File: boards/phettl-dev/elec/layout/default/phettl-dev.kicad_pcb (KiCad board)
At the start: 4 copper layers, 2 parts, among them U1 ?

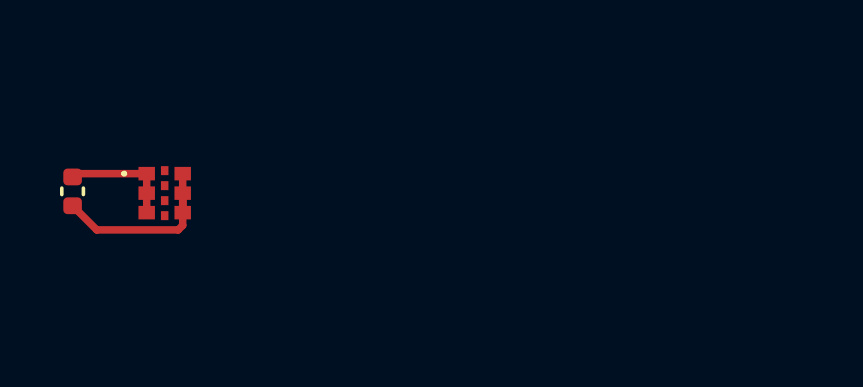
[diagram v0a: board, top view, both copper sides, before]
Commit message: [PART] use better temp sensor
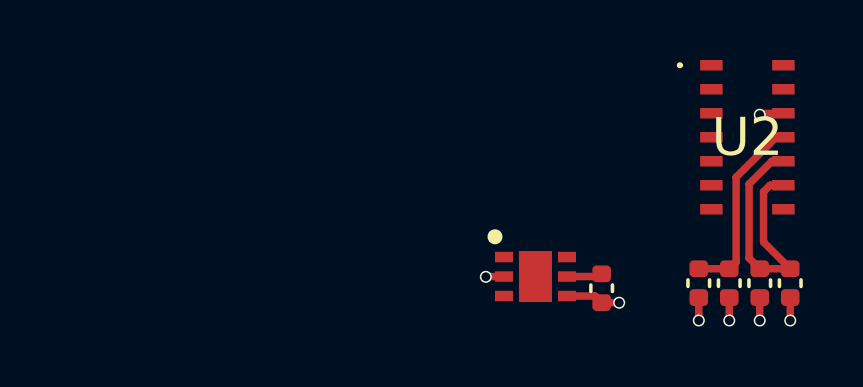
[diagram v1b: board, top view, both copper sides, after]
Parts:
- added C2: 6.3V 10uF X5R ±20% 0402 Multilayer Ceramic Capacitors MLCC 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, lib:C0402, F.Cu at (150.3, 91.9)
- added C3: 16V 100nF X7R ±10% 0402 Multilayer Ceramic Capacitors MLCC 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, lib:C0402, F.Cu at (151.3, 91.9)
- added C4: 10V 4.7uF X5R ±20% 0402 Multilayer Ceramic Capacitors MLCC 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, lib:C0402, F.Cu at (152.4, 91.9)
- added C5: 16V 100nF X7R ±10% 0402 Multilayer Ceramic Capacitors MLCC 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, lib:C0402, F.Cu at (153.4, 91.9)
- added U2: ?, lib:MAX30102EFDT, F.Cu at (151.9, 87.0)
- U1: footprint lib:MAX30208CLBT -> lib:SON65P200X200X80-7N
- moved C1 17.9 mm to (147.1, 92.0)
- moved U1 12.7 mm to (144.9, 91.6)
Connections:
- C1 pad 1: vcc -> temp-vcc
- U1 pad 1: vcc -> temp-scl
- U1 pad 2: vcc -> temp-gnd
- U1 pad 3: vcc -> temp-io
- U1 pad 5: temp-gnd -> temp-vcc
- U1 pad 6: temp-gnd -> temp-sda
- U1 pad 7: temp-io -> ep
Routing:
- net hr-vcc-1: track 0.00 -> 9.13 mm
- net hr-vcc: track 0.00 -> 6.29 mm
- net temp-gnd: track 6.44 -> 2.44 mm, vias 0 -> 2
- net hr-gnd: track 0.00 -> 3.82 mm, vias 0 -> 5
- net vcc: track 3.82 -> 0.00 mm
- net temp-vcc: track 0.00 -> 1.19 mm

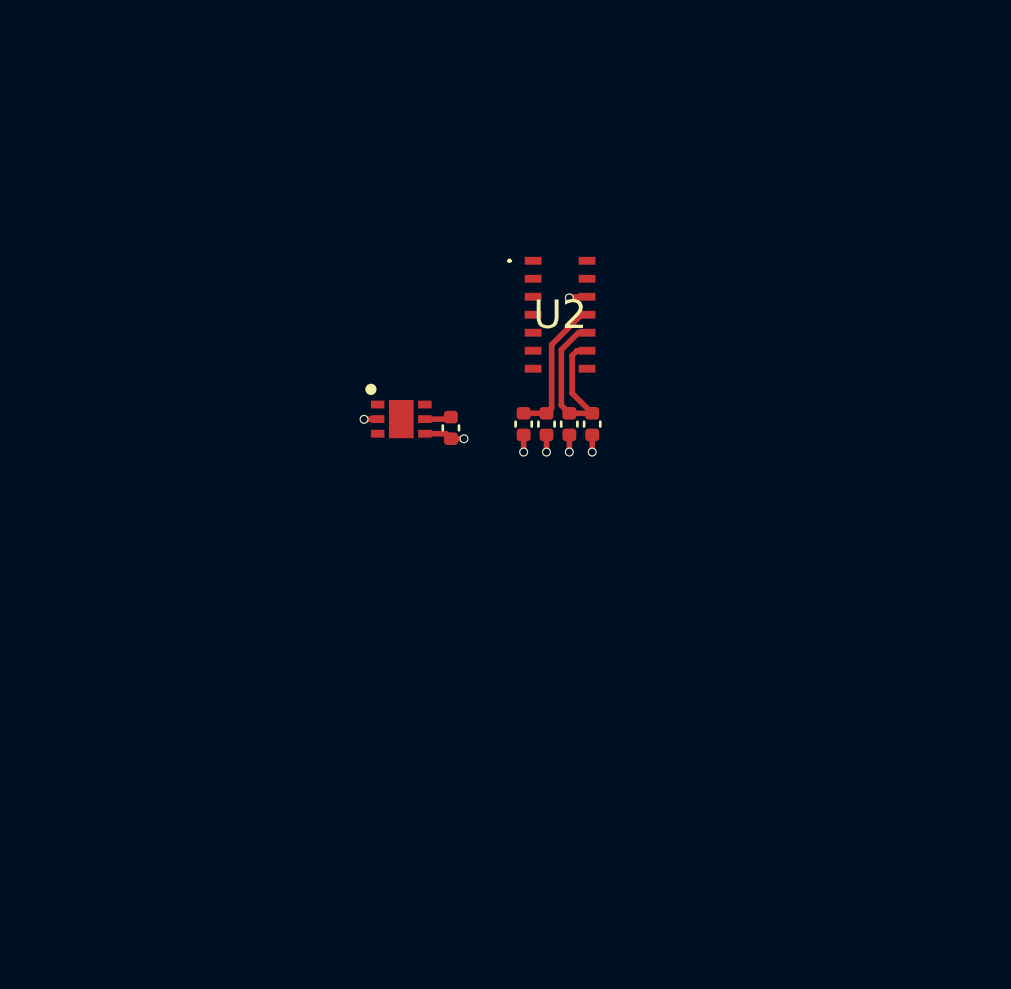
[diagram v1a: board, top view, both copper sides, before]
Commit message: [PART] add xiao
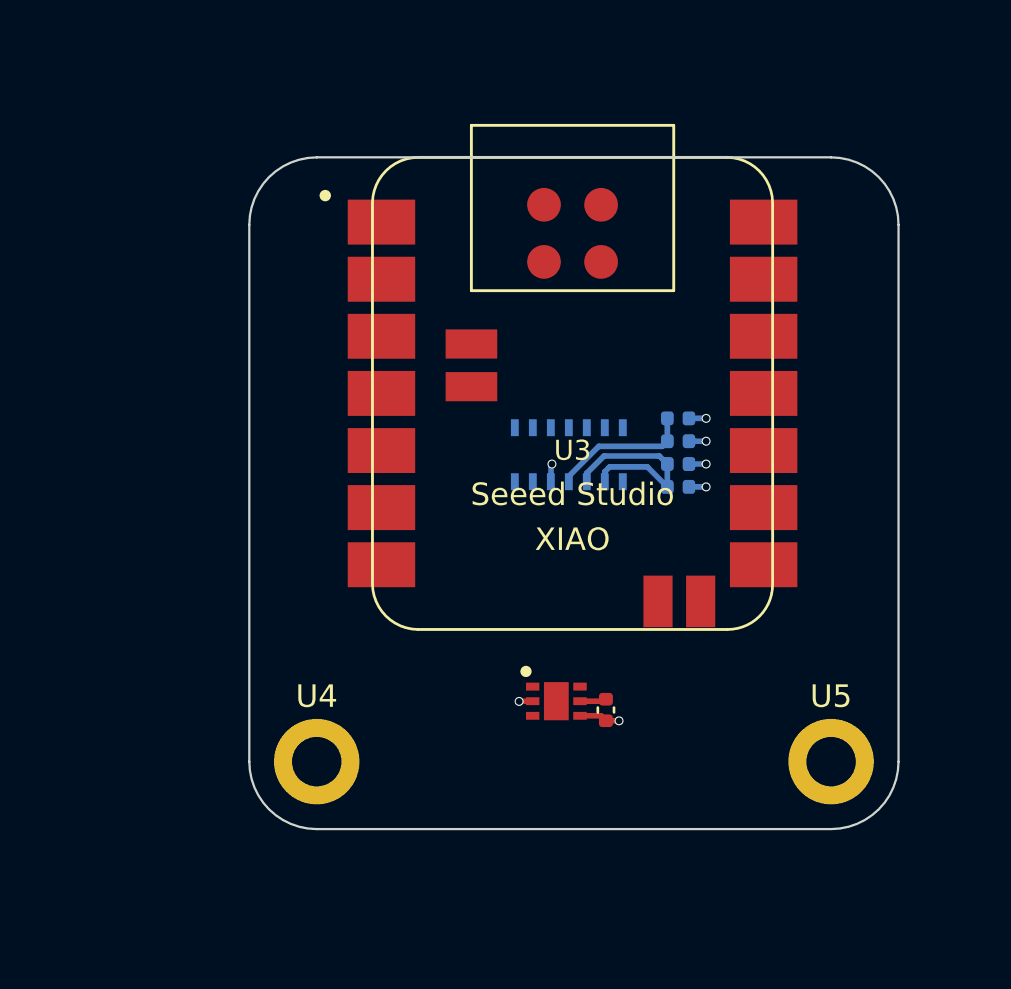
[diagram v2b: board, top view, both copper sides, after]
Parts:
- added U3: ?, lib:XIAO-nRF52840-Sense-14P-2.54-21X17.8MM, F.Cu at (152.5, 90.5)
- added U4: ?, MountingHole:MountingHole_2.2mm_M2_DIN965_Pad, F.Cu at (141.1, 106.9)
- added U5: ?, MountingHole:MountingHole_2.2mm_M2_DIN965_Pad, F.Cu at (164.0, 106.9)
- C2, C3, C4, C5, U2: moved to B.Cu
- moved U1 14.3 mm to (151.8, 104.2)
- moved C1 14.3 mm to (154.0, 104.6)
- moved C2 6.88 mm to (157.2, 91.6), turned to 0 degrees
- moved U2 6.24 mm to (152.3, 93.2), turned to -90 degrees
- moved C3 5.91 mm to (157.2, 92.6), turned to 0 degrees
- moved C4 5.16 mm to (157.2, 93.6), turned to 0 degrees
- moved C5 4.74 mm to (157.2, 94.7), turned to 0 degrees
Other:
- board outline added: 28.9 x 29.9 mm

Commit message: [BOARD] add pullups
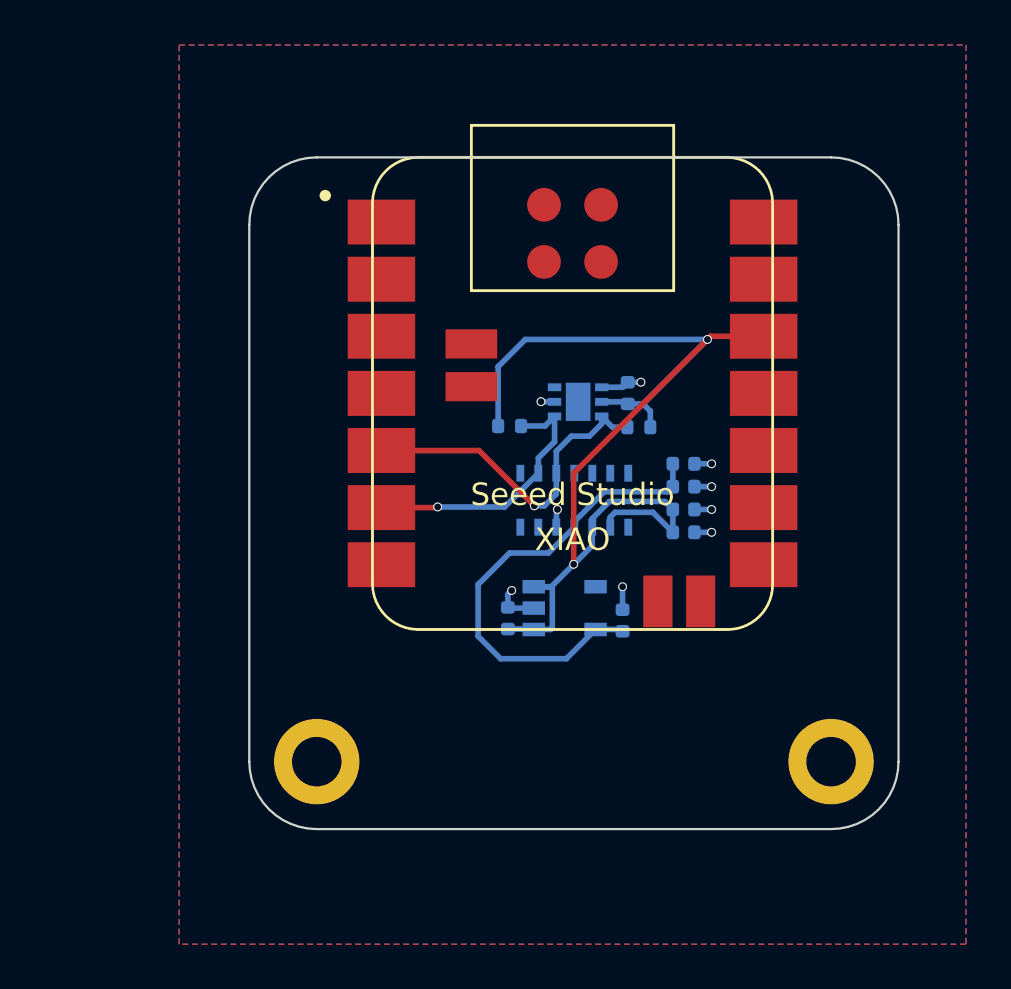
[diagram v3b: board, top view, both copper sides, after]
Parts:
- added C6: 25V 1uF X5R ±10% 0402 Multilayer Ceramic Capacitors MLCC - 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, lib:C0402, B.Cu at (149.6, 100.5)
- added C7: 25V 1uF X5R ±10% 0402 Multilayer Ceramic Capacitors MLCC - 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, lib:C0402, B.Cu at (154.7, 100.6)
- added R1: 62.5mW Thick Film Resistors 50V ±100ppm/℃ ±1% 4.7kΩ 0402 Ch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, lib:R0402, B.Cu at (149.7, 92.0)
- added R2: 62.5mW Thick Film Resistors 50V ±100ppm/℃ ±1% 4.7kΩ 0402 Ch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, lib:R0402, B.Cu at (155.4, 92.0)
- added U6: ?, lib:DBV0005A_N, B.Cu at (152.2, 100.0)
- C1: moved to B.Cu
- U3: renamed from U1; moved to B.Cu
- moved C1 14.1 mm to (155.0, 90.5), turned to 90 degrees
- moved U3 13.4 mm to (152.8, 90.9)
- moved C3 2.04 mm to (157.4, 94.6)
- moved C5 2.04 mm to (157.4, 96.7)
- moved C2 2.04 mm to (157.4, 93.6)
- moved C4 2.04 mm to (157.4, 95.7)
- moved U4 2.04 mm to (152.6, 95.2)
- renumbered U4 to U1, U5 to U2, U2 to U4, U3 to U5
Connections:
- net _5v renamed xiao-vcc
- net batplus renamed vcc
- net hr-vcc renamed vcc-2
- C1 pad 1: temp-vcc -> vcc-1
- C1 pad 2: temp-gnd -> gnd
- C2 pad 2: hr-gnd -> gnd
- C3 pad 2: hr-gnd -> gnd
- C4 pad 1: hr-vcc-1 -> vcc-1
- C4 pad 2: hr-gnd -> gnd
- C5 pad 1: hr-vcc-1 -> vcc-1
- C5 pad 2: hr-gnd -> gnd
- U1 pad 1: m1-gnd -> gnd
- U2 pad 1: m2-gnd -> gnd
- U3 pad 1: temp-scl -> scl
- U3 pad 2: temp-gnd -> gnd
- U3 pad 4: temp-gnd -> gnd
- U3 pad 5: temp-vcc -> vcc-1
- U3 pad 6: temp-sda -> sda
- U4 pad 10: hr-vcc-1 -> vcc-1
- U4 pad 12: hr-gnd -> gnd
- U4 pad 2: hr-scl -> scl
- U4 pad 3: hr-sda -> sda
- U4 pad 9: hr-vcc-1 -> vcc-1
- U5 pad 12: _3v3 -> vcc-1
- U5 pad 13: xiao.ic-gnd -> gnd
- U5 pad 18: xiao.ic-gnd -> gnd
- U5 pad 21: batminus -> gnd
- U5 pad 5: p004_a4_d4_sda -> sda
- U5 pad 6: p005_a5_d5_scl -> scl
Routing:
- net vcc-1: track 0.00 -> 52.5 mm, vias 0 -> 2
- net sda: track 0.00 -> 15.1 mm, vias 0 -> 1
- net vcc-2: track 6.29 -> 21.3 mm
- net scl: track 0.00 -> 12.1 mm, vias 0 -> 1
- net gnd: track 0.00 -> 9.31 mm, vias 0 -> 9
- net hr-vcc-1: track 9.13 -> 0.00 mm
- net hr-gnd: track 3.82 -> 0.00 mm, vias 5 -> 0
- net temp-gnd: track 2.44 -> 0.00 mm, vias 2 -> 0
- net temp-vcc: track 1.19 -> 0.00 mm
- added copper zone on B.Cu, net gnd
- added copper zone on F.Cu, net gnd
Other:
- copper layers 4 -> 2

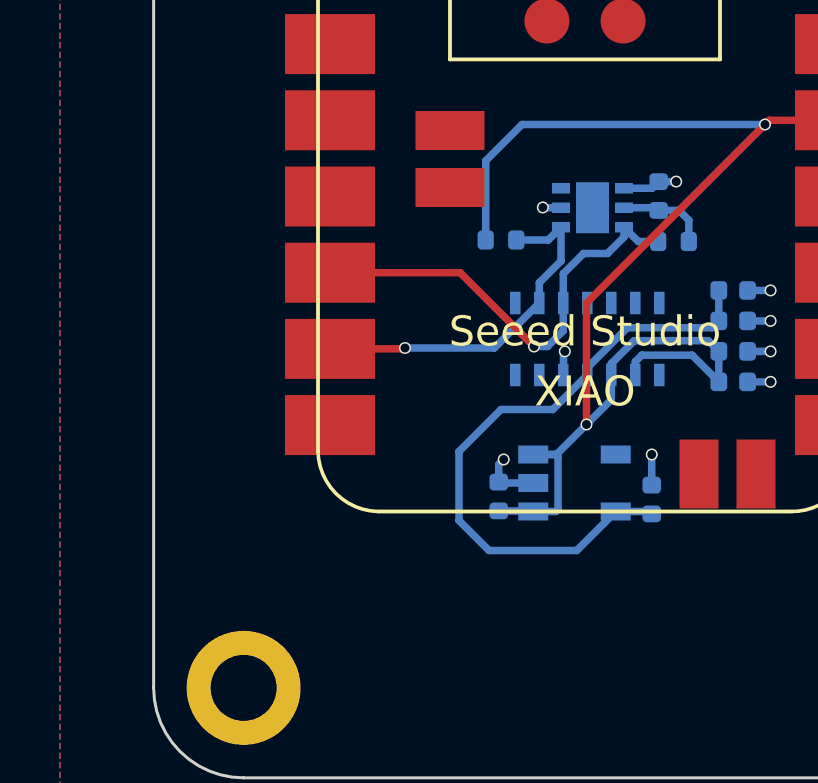
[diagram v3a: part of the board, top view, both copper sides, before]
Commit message: [BAT] add connectors
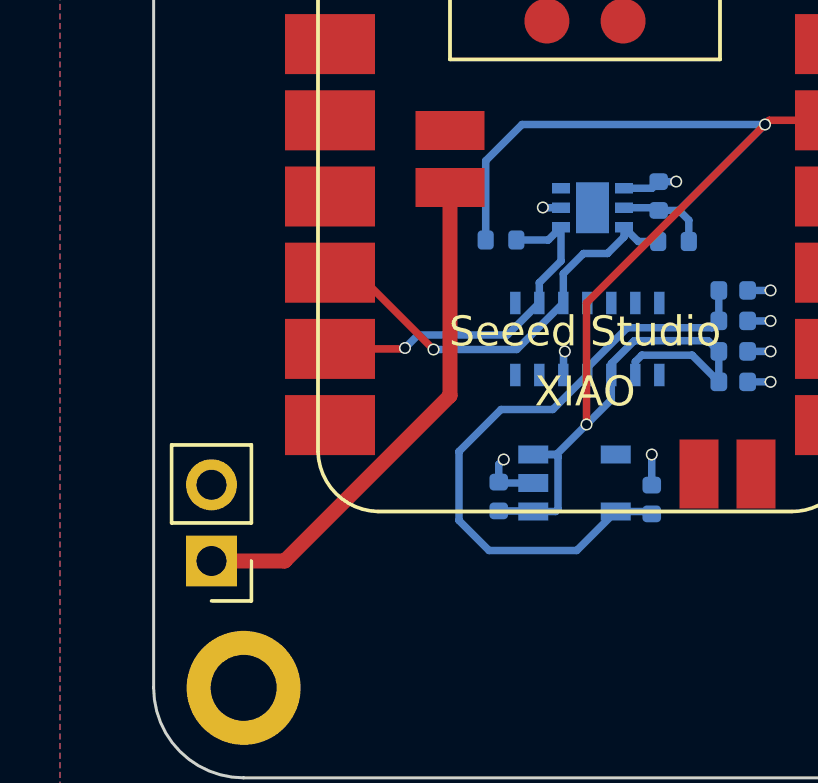
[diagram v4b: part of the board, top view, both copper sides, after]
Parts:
- added U7: ?, Connector_PinHeader_2.54mm:PinHeader_1x02_P2.54mm_Vertical, F.Cu at (140.1, 102.7)
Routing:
- net vcc: track 0.00 -> 17.2 mm
